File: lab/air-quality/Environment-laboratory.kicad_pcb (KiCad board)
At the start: 2 copper layers, 90 x 80 mm, 8 parts, among them U1 atmega328p

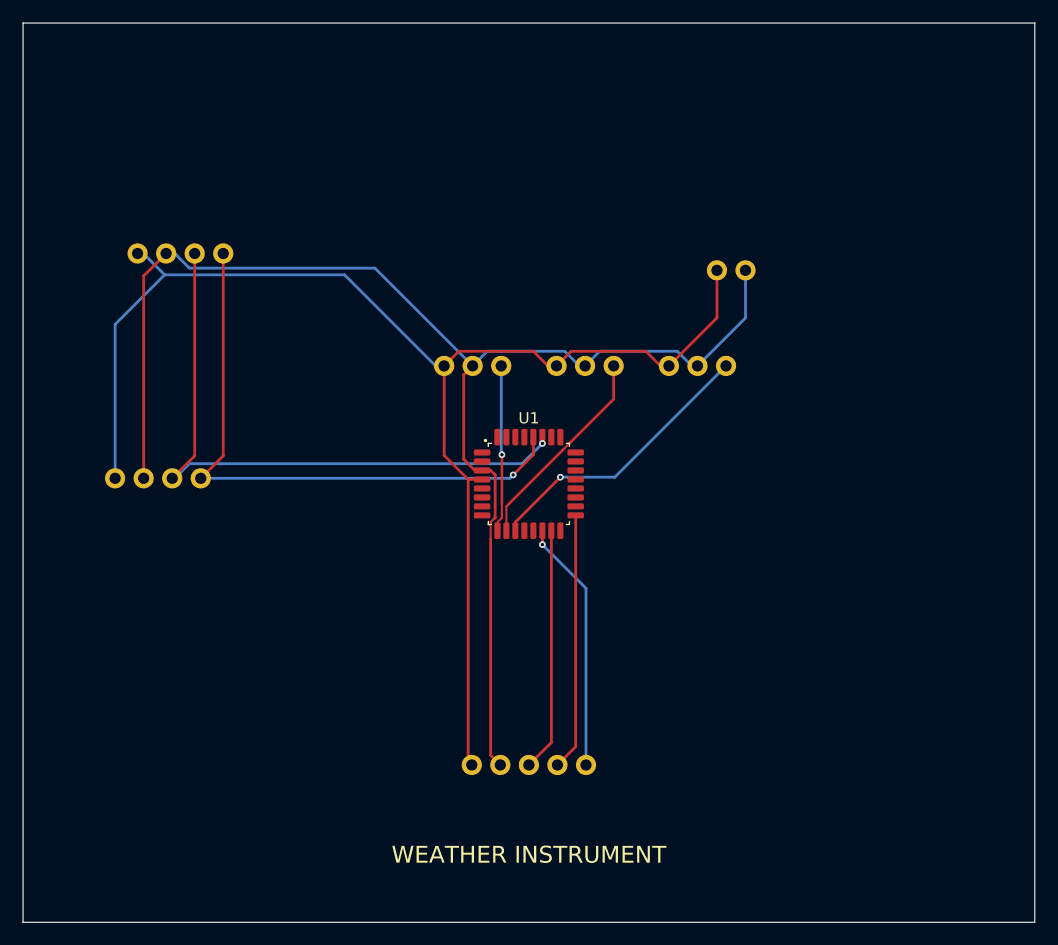
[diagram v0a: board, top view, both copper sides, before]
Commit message: lab: every board is a real board: an Arduino Nano and registry parts, routed, ready to order
The lab boards ran on simulation-only envelopes (labMcu, labDisplay, a battery). Now each is
an Arduino Nano on two sockets on the back (flashed over its USB, the image the app builds),
its lights LEDs through 1 kΩ, its knobs PTV09A pots, its display the MAX7219 eight-digit
module, its sensors an SHT31 and an SCD40 with their datasheets' support circuits, the FTDI
header for the serial console; the servo boards take 5 V on a screw terminal with a bulk
capacitor. All ten check complete with no errors or warnings, their firmware unchanged
(serial-device now on the 328P), and run in the lab without a fault (3 s each, dev host).

The registry: every interactive board must be ready to order and flash (publish.mjs refuses
one that is not; status simulation-only removed).

Claude-Session: https://claude.ai/code/session_01ATmMmxyrWxFwR3nTdXUrcx
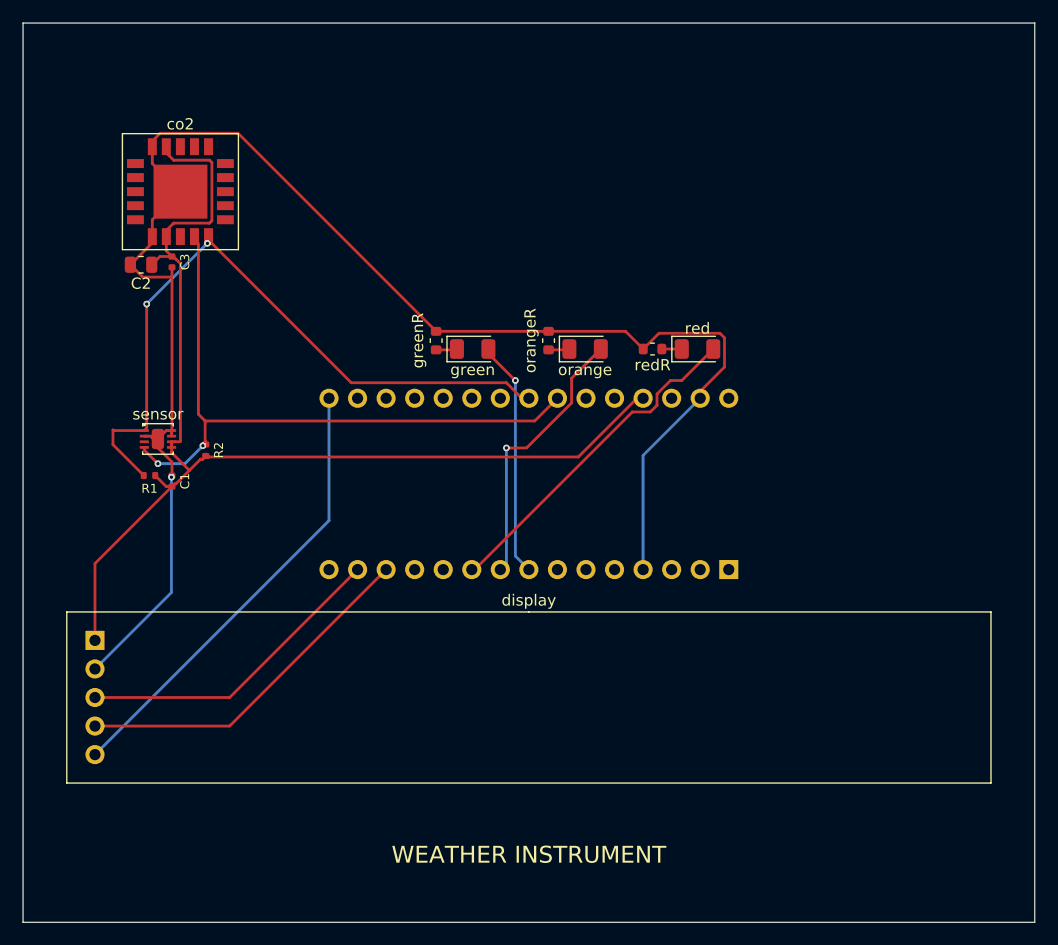
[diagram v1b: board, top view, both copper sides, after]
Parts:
- removed battery: battery, Regulated battery module
- removed the display at (145.0, 180.0)
- removed the green at (140.0, 149.0)
- removed the orange at (150.0, 149.0)
- removed the red at (160.0, 149.0)
- removed the sensor at (112.0, 157.0)
- added C1: 100nF, C_0402_1005Metric, F.Cu at (113.2, 160.8)
- added C2: 10uF, C_0805_2012Metric, F.Cu at (110.5, 141.5)
- added C3: 100nF, C_0402_1005Metric, F.Cu at (113.2, 141.2)
- added R1: 10kohm, R_0402_1005Metric, F.Cu at (111.2, 160.2)
- added R2: 10kohm, R_0402_1005Metric, F.Cu at (116.2, 158.0)
- added display: MAX7219 8-digit 7-segment LED display module, MAX7219_8digit_Module_Socket_1x05_P2.54mm, F.Cu at (145.0, 180.0)
- added green: green, LED_1206_3216Metric, F.Cu at (140.0, 149.0)
- added greenR: 1kohm, R_0603_1608Metric, F.Cu at (136.8, 148.2)
- added orange: orange, LED_1206_3216Metric, F.Cu at (150.0, 149.0)
- added orangeR: 1kohm, R_0603_1608Metric, F.Cu at (146.8, 148.2)
- added red: red, LED_1206_3216Metric, F.Cu at (160.0, 149.0)
- added redR: 1kohm, R_0603_1608Metric, F.Cu at (156.0, 149.0)
- added sensor: SHT31-DIS-B2.5kS, DFN-8-1EP_2.5x2.5mm_P0.5mm_EP1.1x1.8mm, F.Cu at (112.0, 157.0)
- U1: value atmega328p -> A000005; footprint TQFP-32_7x7mm_P0.8mm -> Arduino_Nano_Socket_2x15_P2.54mm_W15.24mm; moved to B.Cu
- co2: value scd40 -> SCD40-D-R2; footprint SCD40 module -> LGA-21_10.1x10.1mm_SCD4x_20_pads_and_a_centre_pad
- turned U1 to 90 degrees
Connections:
- U1 pad 10: ORANGE -> RED
- U1 pad 11: RED -> (no net)
- U1 pad 13: (no net) -> LOAD
- U1 pad 14: LOAD -> MOSI
- U1 pad 15: MOSI -> (no net)
- U1 pad 16: (no net) -> SCK
- U1 pad 17: SCK -> (no net)
- U1 pad 23: (no net) -> SDA
- U1 pad 24: (no net) -> SCL
- U1 pad 27: SDA -> V5
- U1 pad 28: SCL -> (no net)
- U1 pad 29: (no net) -> GND
- U1 pad 3: GND -> (no net)
- U1 pad 4: V5 -> GND
- U1 pad 8: (no net) -> GREEN
- U1 pad 9: GREEN -> ORANGE
- co2 pad 1: V5 -> (no net)
- co2 pad 2: GND -> (no net)
- co2 pad 3: SDA -> (no net)
- co2 pad 4: SCL -> (no net)
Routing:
- net GND: track 123.0 -> 144.4 mm, vias 0 -> 1
- net SCK: track 22.9 -> 40.3 mm
- net V5: track 119.7 -> 103.7 mm
- net LOAD: track 22.4 -> 31.7 mm, vias 1 -> 0
- net MOSI: track 21.7 -> 28.1 mm
- net GREEN: track 14.9 -> 21.1 mm
- net ORANGE: track 18.6 -> 24.4 mm, vias 0 -> 1
- net SDA: track 55.0 -> 60.0 mm, vias 1 -> 2
- net RED: track 25.3 -> 30.2 mm, vias 1 -> 0
- net SCL: track 52.9 -> 57.3 mm, vias 1 -> 2
- net GREEN_K: track 0.00 -> 2.09 mm
- net ORANGE_K: track 0.00 -> 1.88 mm
- net RED_K: track 0.00 -> 1.78 mm

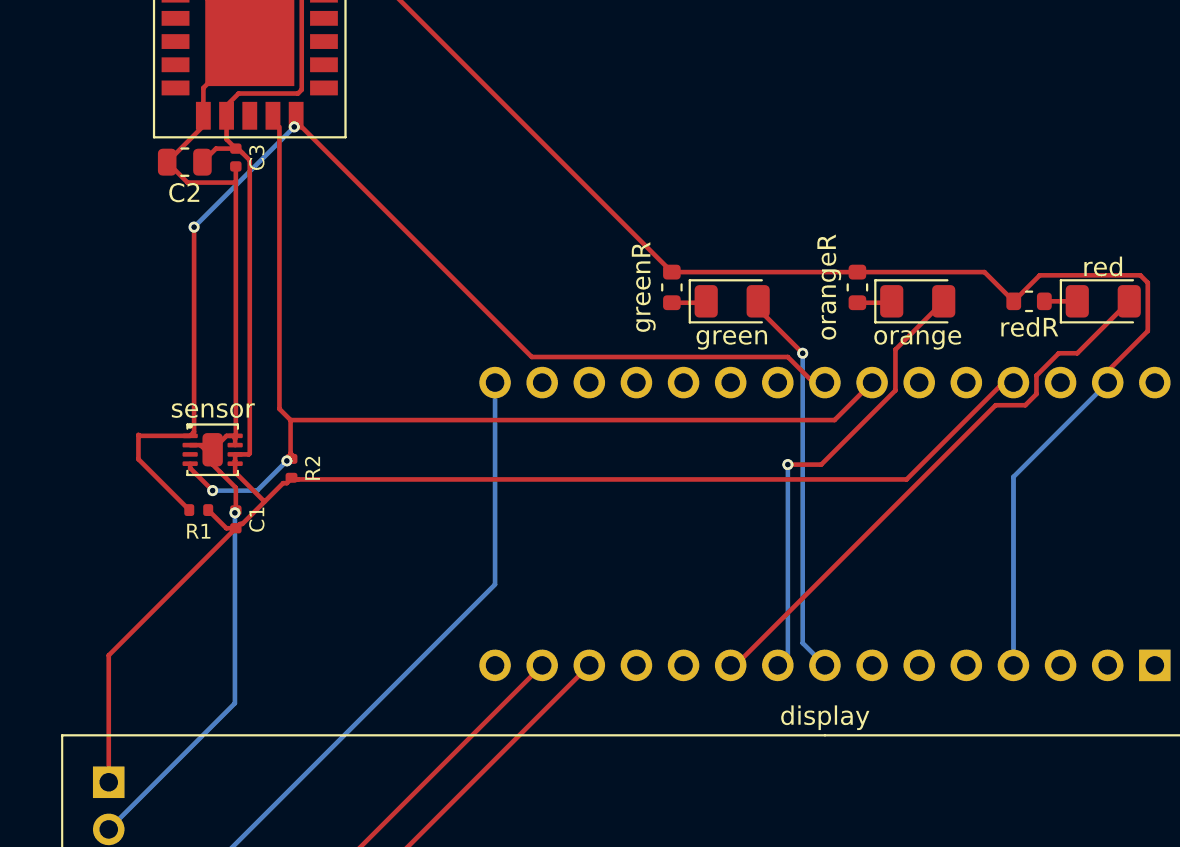
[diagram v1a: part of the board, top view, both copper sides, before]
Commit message: registry: every board rebuilt with pcbkit main 4684674e6 - the bought part named on the board
pcbkit dc07fdfd6 writes the bought row's MPN and Manufacturer (the design's own kept as DesignMPN /
DesignManufacturer) and the build chooses parts before it places (6361ec104). Each of the 44 boards
was rebuilt (; the two P4 boards  only: their builds reroute pairs):
copper unchanged on all 44 (segments, arcs and vias counted before and after), placement kept; the
Arduino and lab boards now carry the parts the catalogue gives them. The check gains only the new
judgements: part-maker (a part bought from another maker) and part-missing on hand-fitted modules
(DS1 sockets); p4-touch-7 loses part-stale. The P4 boards keep their hole-clearance errors (a
reroute is Team 3's).

Claude-Session: https://claude.ai/code/session_01BAgp959tApA8aEg85EYgfb
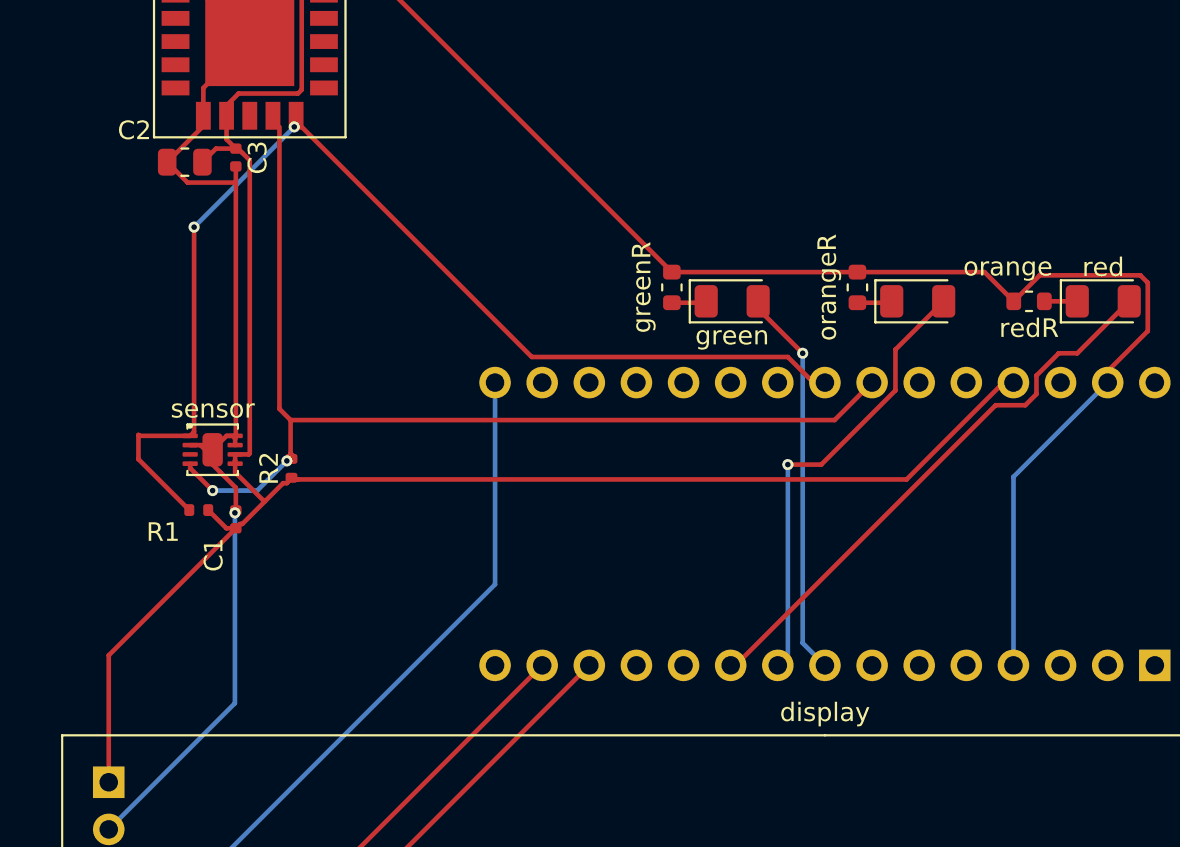
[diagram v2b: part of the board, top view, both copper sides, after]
